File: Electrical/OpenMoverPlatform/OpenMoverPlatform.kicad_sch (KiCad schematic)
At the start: 7 parts, among them J1 battery supply, J2 BLDC1 power, J3 BLDC2 power, U1 ESP32-S3-WROOM-2

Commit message: swx update
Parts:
- removed U1: ESP32-S3-WROOM-2, RF_Module:ESP32-S3-WROOM-2, symbol RF_Module:ESP32-S3-WROOM-2
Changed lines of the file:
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@@
-	)
-	(symbol
-		(lib_id "RF_Module:ESP32-S3-WROOM-2")
-		(at 195.58 85.09 0)
-		(unit 1)
-		(exclude_from_sim no)
-		(in_bom yes)
-		(on_board yes)
-		(dnp no)
-		(fields_autoplaced yes)
-		(property "Reference" "U1"
-			(at 197.7741 34.29 0)
-			(effects
-				(font
-					(size 1.27 1.27)
-				)
-				(justify left)
-			)
-		)
-		(property "Value" "ESP32-S3-WROOM-2"
-			(at 197.7741 36.83 0)
-			(effects
-				(font
-					(size 1.27 1.27)
-				)
-				(justify left)
-			)
-		)
-		(property "Footprint" "RF_Module:ESP32-S3-WROOM-2"
-			(at 195.58 146.05 0)
-			(effects
-				(font
-					(size 1.27 1.27)
-				)
-				(hide yes)
-			)
-		)
-		(property "Datasheet" "https://www.espressif.com/sites/default/files/documentation/esp32-s3-wroom-2_datasheet_en.pdf"
-			(at 195.58 148.59 0)
-			(effects
-				(font
-					(size 1.27 1.27)
-				)
-				(hide yes)
-			)
-		)
-		(property "Description" "RF Module, 2.4 GHz, Wi­-Fi, Bluetooth, BLE, ESP32­-S3R8V"
-			(at 195.58 85.09 0)
-			(effects
-				(font
-					(size 1.27 1.27)
-				)
-				(hide yes)
-			)
-		)
-		(pin "8"
-		)
-		(pin "29"
-		)
-		(pin "28"
-		)
-		(pin "2"
-		)
-		(pin "32"
-		)
-		(pin "19"
-		)
-		(pin "17"
-		)
-		(pin "16"
-		)
-		(pin "34"
-		)
-		(pin "22"
-		)
-		(pin "10"
-		)
-		(pin "38"
-		)
-		(pin "23"
-		)
-		(pin "3"
-		)
-		(pin "4"
-		)
-		(pin "33"
-		)
-		(pin "40"
-		)
-		(pin "39"
-		)
-		(pin "41"
-		)
-		(pin "25"
-		)
-		(pin "27"
-		)
-		(pin "26"
-		)
-		(pin "6"
-		)
-		(pin "30"
-		)
-		(pin "11"
-		)
-		(pin "14"
-		)
-		(pin "5"
-		)
-		(pin "15"
-		)
-		(pin "35"
-		)
-		(pin "36"
-		)
-		(pin "31"
-		)
-		(pin "13"
-		)
-		(pin "24"
-		)
-		(pin "9"
-		)
-		(pin "18"
-		)
-		(pin "1"
-		)
-		(pin "37"
-		)
-		(pin "12"
-		)
-		(pin "7"
-		)
-		(pin "20"
-		)
-		(pin "21"
-		)
-		(instances
-			(project "OpenMoverPlatform"
-				(path "/52699ea0-1640-4cca-8cb0-8bacf65a023c"
-					(reference "U1")
-					(unit 1)
-				)
-			)
-		)
 	)
 	(symbol

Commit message: control pcb v1
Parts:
- added C1: C_Polarized, Capacitor_SMD:CP_Elec_8x10.5, symbol Device:C_Polarized
- added C2: C, Capacitor_SMD:CP_Elec_8x10.5, symbol Device:C_Polarized
- added C3, C4: C, Capacitor_SMD:C_1210_3225Metric_Pad1.33x2.70mm_HandSolder, symbol Device:C
- added D1: D_Schottky, Diode_SMD:D_SMA-SMB_Universal_Handsoldering, symbol Device:D_Schottky
- added H1, H2, H3: MountingHole, MountingHole:MountingHole_3.2mm_M3, symbol Mechanical:MountingHole
- added J4: GPS_MAG, Connector_PinHeader_2.54mm:PinHeader_1x06_P2.54mm_Vertical, symbol Connector:Conn_01x06_Pin
- added J5: I2C_1, Connector_PinHeader_2.54mm:PinHeader_1x04_P2.54mm_Vertical, symbol Connector:Conn_01x04_Pin
- added J6: BLDC1 PWM, Connector_PinHeader_2.54mm:PinHeader_1x03_P2.54mm_Vertical, symbol Connector:Conn_01x03_Pin
- added J7: BLDC2 PWM, Connector_PinHeader_2.54mm:PinHeader_1x03_P2.54mm_Vertical, symbol Connector:Conn_01x03_Pin
- added J8: I2C_2, Connector_PinHeader_2.54mm:PinHeader_1x04_P2.54mm_Vertical, symbol Connector:Conn_01x04_Pin
- added J9: MOD_SERIAL, Connector_PinHeader_2.54mm:PinHeader_1x04_P2.54mm_Vertical, symbol Connector:Conn_01x04_Pin
- added JP1: Regulator Adj, Jumper:SolderJumper-2_P1.3mm_Open_TrianglePad1.0x1.5mm, symbol Jumper:SolderJumper_2_Open
- added JP2: 3V3_Disconnect, Jumper:SolderJumper-2_P1.3mm_Open_TrianglePad1.0x1.5mm, symbol Jumper:SolderJumper_2_Open
- added JP3: 3V3_Disconnect_B, Connector_PinHeader_2.54mm:PinHeader_2x01_P2.54mm_Vertical, symbol Jumper:Jumper_2_Open
- added L1: L, Inductor_SMD:L_Bourns_SRR1260, symbol Device:L
- added R1, R2, R3, R4, R5, R6: R, Resistor_SMD:R_1206_3216Metric_Pad1.30x1.75mm_HandSolder, symbol Device:R
- added U1: WeMos_LoLin32_Lite, customFootprints:lolin32lite, symbol customSymbols:WeMos_LoLin32_Lite
- added U2: LM2596S-ADJ, Package_TO_SOT_SMD:TO-263-5_TabPin3, symbol Regulator_Switching:LM2596S-ADJ
- F1: renamed from F3; footprint (none) -> Fuse:Fuseholder_Blade_Mini_Keystone_3568
- F2: footprint (none) -> Fuse:Fuseholder_Blade_Mini_Keystone_3568
- F3: renamed from F1; footprint (none) -> Fuse:Fuseholder_Blade_Mini_Keystone_3568
- J2: value BLDC1 power -> BLDC1 POWER
- J3: value BLDC2 power -> BLDC2 POWER
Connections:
- net +BATT: now also C2.1, C3.1, R1.1, U2.1 (VIN)
- net GND: now also C1.2, C2.2, C3.2, D1.2 (A), J4.1 (Pin_1), J5.4 (Pin_4), J6.2 (Pin_2), J7.2 (Pin_2), J8.4 (Pin_4), J9.4 (Pin_4), R4.2, R6.1, U1.26 (GND), U2.3 (GND), U2.5 (~{ON}/OFF)
- new net: C1.1, C4.2, JP1.1 (A), JP2.1 (A), JP3.1 (A), L1.2, R5.2
- new net: C4.1, JP1.2 (B), R5.1, R6.2, U2.4 (FB)
- new net: R1.2, R2.1
- new net: R2.2, R3.1
- new net: D1.1 (K), L1.1, U2.2 (OUT)
- new net +3V3: J4.4 (Pin_4), J5.1 (Pin_1), J8.1 (Pin_1), J9.1 (Pin_1), JP2.2 (B), JP3.2 (B), U1.13 (3v3)
- new net IO12_PWM1: J6.3 (Pin_3), U1.25 (GPIO12)
- new net IO13_PWM2: J7.3 (Pin_3), U1.1 (GPIO13)
- new net IO14_BatADC: R3.2, R4.1, U1.24 (GPIO14)
- new net IO16_RXGPS: J4.2 (Pin_2), U1.6 (GPIO16)
- new net IO17_TXGPS: J4.3 (Pin_3), U1.7 (GPIO17)
- new net IO18_SDA: J4.5 (Pin_5), J5.2 (Pin_2), J8.2 (Pin_2), U1.9 (GPIO18)
- new net IO23_SCL: J4.6 (Pin_6), J5.3 (Pin_3), J8.3 (Pin_3), U1.10 (GPIO23)
- new net IO4_RXMOD: J9.3 (Pin_3), U1.5 (GPIO04)
- new net IO5_TXMOD: J9.2 (Pin_2), U1.8 (GPIO05)
- no-connect marks 0 -> 2
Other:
- note added: "Battery Voltage Divider"
- note added: "Interfaces"
- note added: "Logic Voltage Regulator"
- note added: "Supply"
- moved on the sheet: J2, J3

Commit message: ki cad pcb update
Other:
- note added: "Mechanical"
- moved on the sheet: H1, H2, H3
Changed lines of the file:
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@@
 		)
 	)
+	(polyline
+		(pts
+			(xy 240.03 71.12) (xy 284.48 71.12)
+		)
+		(stroke
+			(width 0)
+			(type default)
+		)
+	)
 	(wire
 		(pts
@@
 		)
 	)
+	(text "Mechanical"
+		(exclude_from_sim no)
+		(at 224.028 15.494 0)
+		(effects
+			(font
+				(size 1.27 1.27)
+			)
+		)
+	)
 	(text "Logic Voltage Regulator\n"
 		(exclude_from_sim no)
@@
 	(symbol
 		(lib_id "Mechanical:MountingHole")
-		(at 241.3 30.48 0)
+		(at 248.92 41.91 0)
 		(unit 1)
 		(exclude_from_sim yes)
@@
 		(fields_autoplaced yes)
 		(property "Reference" "H2"
-			(at 243.84 29.2099 0)
+			(at 251.46 40.6399 0)
 			(effects
 				(font
@@
 		)
 		(property "Value" "MountingHole"
-			(at 243.84 31.7499 0)
+			(at 251.46 43.1799 0)
 			(effects
 				(font
@@
 		)
 		(property "Footprint" "MountingHole:MountingHole_3.2mm_M3"
-			(at 241.3 30.48 0)
+			(at 248.92 41.91 0)
 			(effects
 				(font
@@
 		)
 		(property "Datasheet" "~"
-			(at 241.3 30.48 0)
+			(at 248.92 41.91 0)
 			(effects
 				(font
@@
 		)
 		(property "Description" "Mounting Hole without connection"
-			(at 241.3 30.48 0)
+			(at 248.92 41.91 0)
 			(effects
 				(font
@@
 	(symbol
 		(lib_id "Mechanical:MountingHole")
-		(at 241.3 24.13 0)
+		(at 248.92 35.56 0)
 		(unit 1)
 		(exclude_from_sim yes)
@@
 		(fields_autoplaced yes)
 		(property "Reference" "H1"
-			(at 243.84 22.8599 0)
+			(at 251.46 34.2899 0)
 			(effects
 				(font
@@
 		)
 		(property "Value" "MountingHole"
-			(at 243.84 25.3999 0)
+			(at 251.46 36.8299 0)
 			(effects
 				(font
@@
 		)
 		(property "Footprint" "MountingHole:MountingHole_3.2mm_M3"
-			(at 241.3 24.13 0)
+			(at 248.92 35.56 0)
 			(effects
 				(font
@@
 		)
 		(property "Datasheet" "~"
-			(at 241.3 24.13 0)
+			(at 248.92 35.56 0)
 			(effects
 				(font
@@
 		)
 		(property "Description" "Mounting Hole without connection"
-			(at 241.3 24.13 0)
+			(at 248.92 35.56 0)
 			(effects
 				(font
@@
 	(symbol
 		(lib_id "Mechanical:MountingHole")
-		(at 241.3 36.83 0)
+		(at 248.92 48.26 0)
 		(unit 1)
 		(exclude_from_sim yes)
@@
 		(fields_autoplaced yes)
 		(property "Reference" "H3"
-			(at 243.84 35.5599 0)
+			(at 251.46 46.9899 0)
 			(effects
 				(font
@@
 		)
 		(property "Value" "MountingHole"
-			(at 243.84 38.0999 0)
+			(at 251.46 49.5299 0)
 			(effects
 				(font
@@
 		)
 		(property "Footprint" "MountingHole:MountingHole_3.2mm_M3"
-			(at 241.3 36.83 0)
+			(at 248.92 48.26 0)
 			(effects
 				(font
@@
 		)
 		(property "Datasheet" "~"
-			(at 241.3 36.83 0)
+			(at 248.92 48.26 0)
 			(effects
 				(font
@@
 		)
 		(property "Description" "Mounting Hole without connection"
-			(at 241.3 36.83 0)
+			(at 248.92 48.26 0)
 			(effects
 				(font

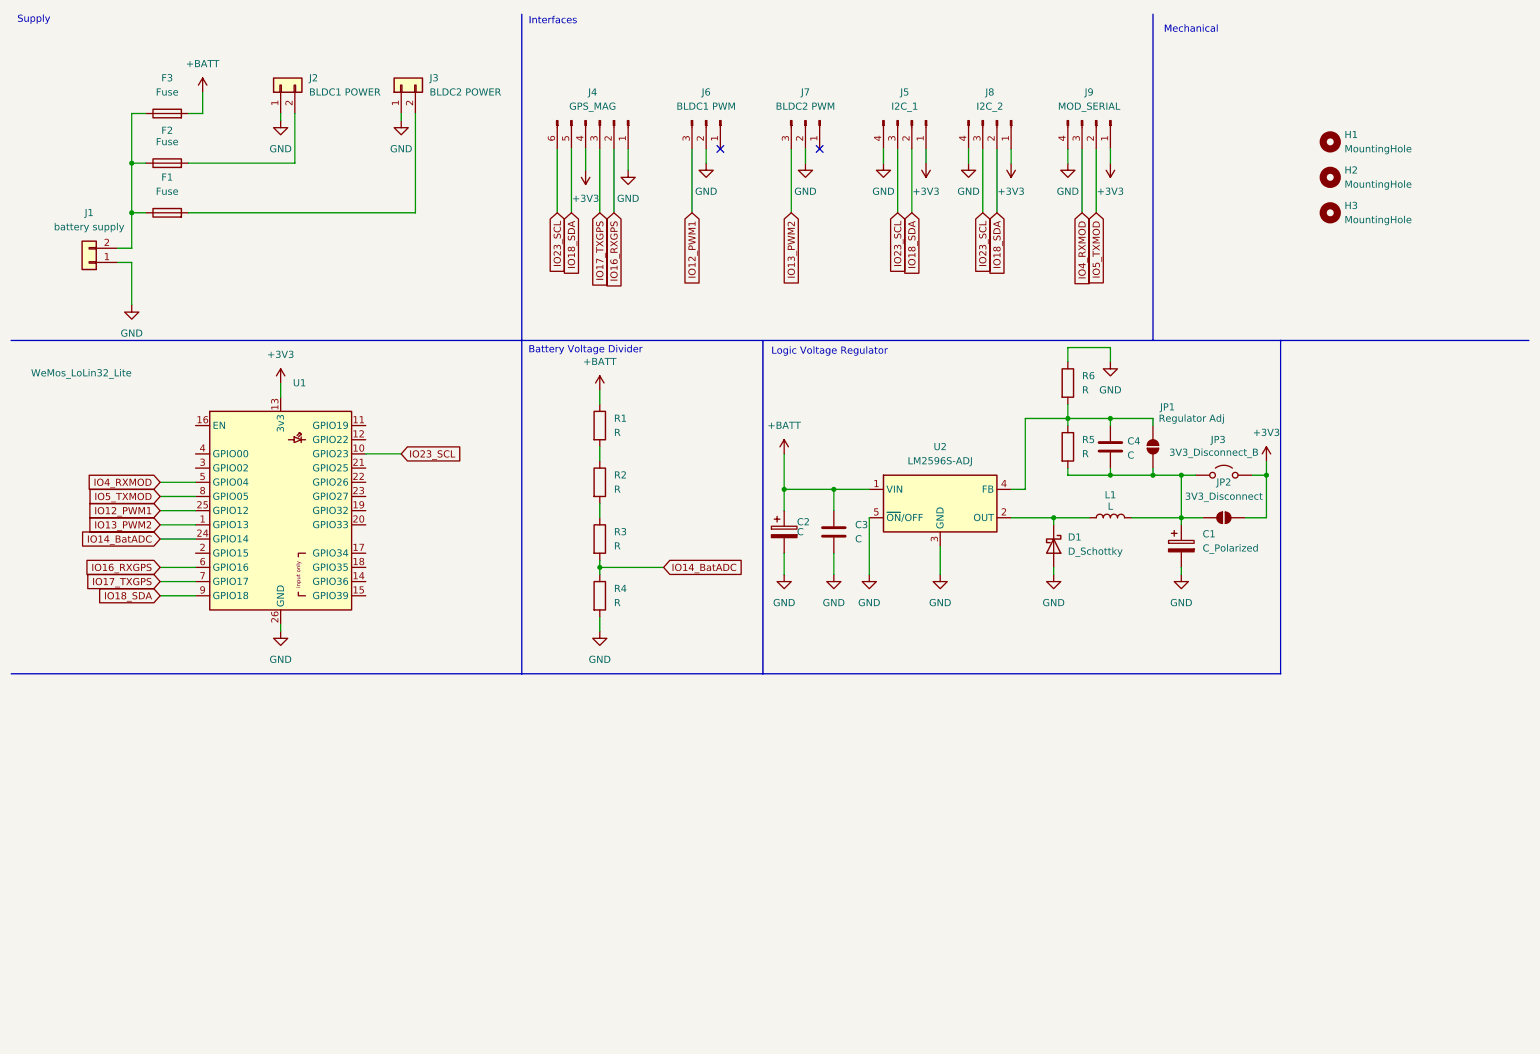
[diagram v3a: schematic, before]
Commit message: updated pcb to use esp32 s3 wroom 1
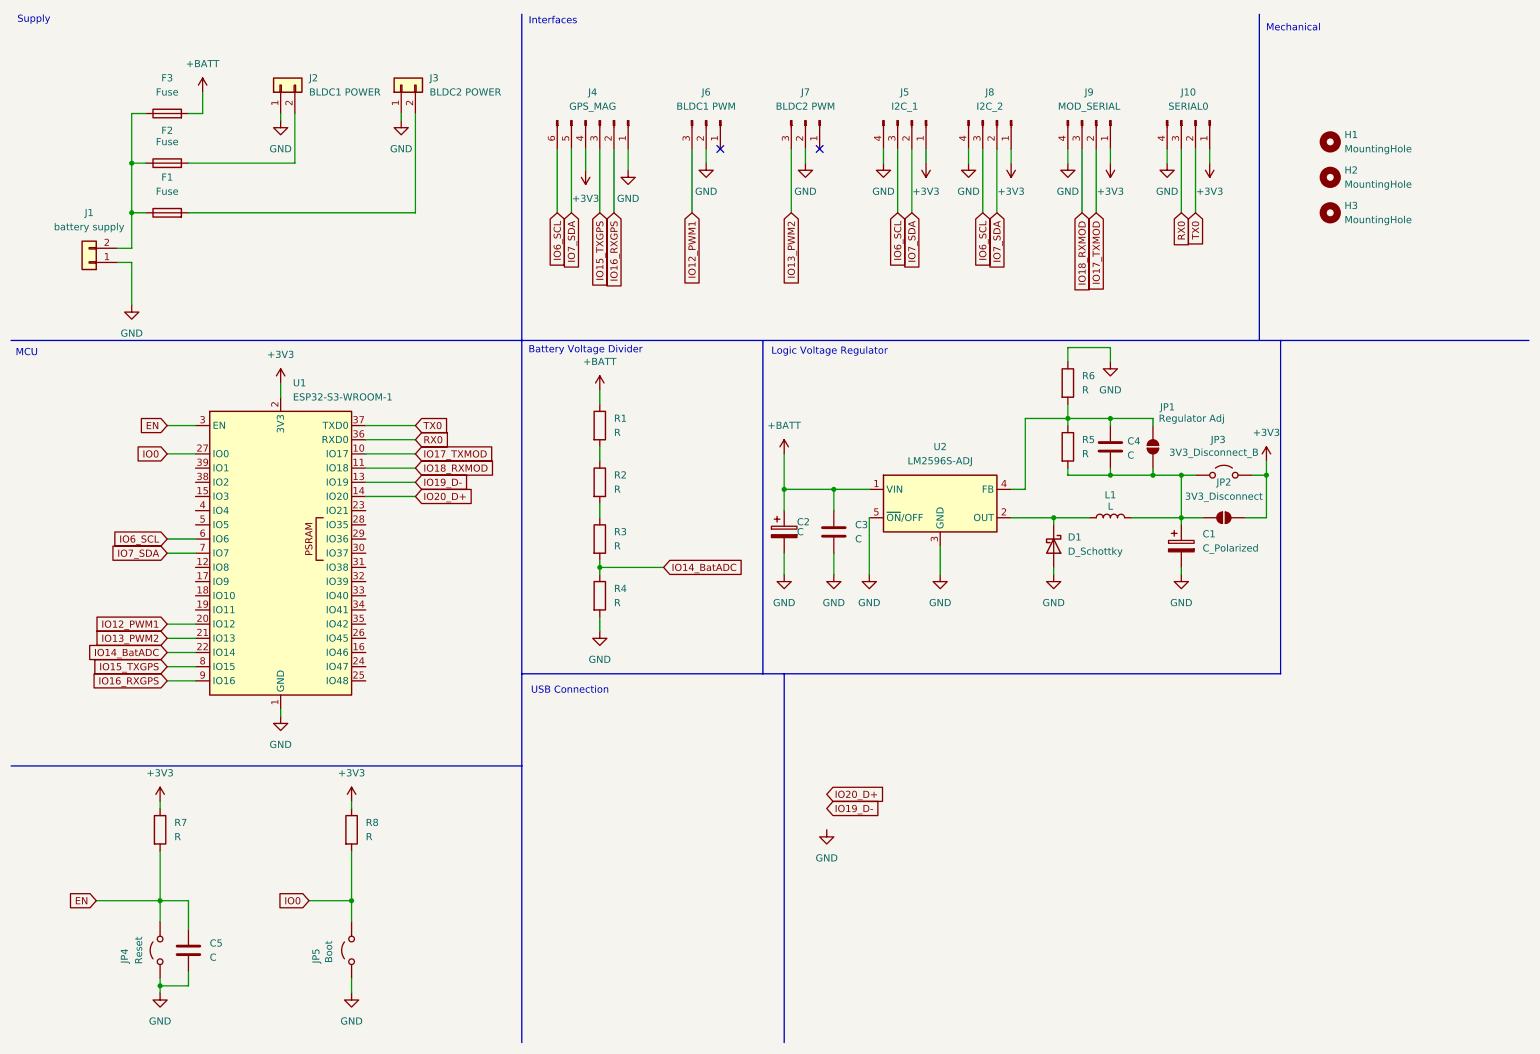
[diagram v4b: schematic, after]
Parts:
- removed U1: WeMos_LoLin32_Lite, customFootprints:lolin32lite, symbol customSymbols:WeMos_LoLin32_Lite
- added C5: C, Capacitor_SMD:C_1210_3225Metric_Pad1.33x2.70mm_HandSolder, symbol Device:C
- added J10: SERIAL0, Connector_PinHeader_2.54mm:PinHeader_1x04_P2.54mm_Vertical, symbol Connector:Conn_01x04_Pin
- added JP4: Reset, Connector_PinHeader_2.54mm:PinHeader_2x01_P2.54mm_Vertical, symbol Jumper:Jumper_2_Open
- added JP5: Boot, Connector_PinHeader_2.54mm:PinHeader_2x01_P2.54mm_Vertical, symbol Jumper:Jumper_2_Open
- added R7, R8: R, Resistor_SMD:R_1206_3216Metric_Pad1.30x1.75mm_HandSolder, symbol Device:R
- added U1: ESP32-S3-WROOM-1, RF_Module:ESP32-S3-WROOM-1, symbol RF_Module:ESP32-S3-WROOM-1
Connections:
- net +3V3: now also J10.1 (Pin_1), R7.1, R8.1, U1.2 (3V3)
- net GND: now also C5.2, J10.4 (Pin_4), JP4.1 (A), JP5.1 (A), U1.1 (GND), U1.40 (GND), U1.41 (GND)
- net IO12_PWM1: now also U1.20 (IO12)
- net IO13_PWM2: now also U1.21 (IO13)
- net IO14_BatADC: now also U1.22 (IO14)
- net IO16_RXGPS: now also U1.9 (IO16)
- net IO17_TXGPS renamed IO15_TXGPS
- net IO15_TXGPS: now also U1.8 (IO15)
- net IO18_SDA renamed IO7_SDA
- net IO7_SDA: now also U1.7 (IO7)
- net IO23_SCL renamed IO6_SCL
- net IO6_SCL: now also U1.6 (IO6)
- net IO4_RXMOD renamed IO18_RXMOD
- net IO18_RXMOD: now also U1.11 (IO18)
- net IO5_TXMOD renamed IO17_TXMOD
- net IO17_TXMOD: now also U1.10 (IO17)
- new net EN: C5.1, JP4.2 (B), R7.2, U1.3 (EN)
- new net IO0: JP5.2 (B), R8.2, U1.27 (IO0)
- new net IO19_D-: U1.13 (IO19)
- new net IO20_D+: U1.14 (IO20)
- new net RX0: J10.3 (Pin_3), U1.36 (RXD0)
- new net TX0: J10.2 (Pin_2), U1.37 (TXD0)
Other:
- note added: "MCU"
- note added: "USB Connection"

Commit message: update 2025
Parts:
- added C6: C, Capacitor_SMD:C_1210_3225Metric_Pad1.33x2.70mm_HandSolder, symbol Device:C
- added J11: USB_B, Connector_USB:USB_B_OST_USB-B1HSxx_Horizontal, symbol Connector:USB_B
- C1: value C_Polarized -> C
- F1, F2, F3: footprint Fuse:Fuseholder_Blade_Mini_Keystone_3568 -> Fuse:Fuse_Blade_Mini_directSolder
- L1: value L -> 47uH
- R1, R2, R3, R4, R7, R8: value R -> 10k
- R5: value R -> 4.2k
- R6: value R -> 2.5k
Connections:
- net +3V3: now also C6.1
- net GND: now also C6.2, J11.4 (GND), J11.5 (Shield)
- net IO19_D-: now also J11.2 (D-)
- net IO20_D+: now also J11.3 (D+)
- no-connect marks 2 -> 3
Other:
- moved on the sheet: JP2, JP3
